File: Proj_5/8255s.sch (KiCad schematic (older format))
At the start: 6 parts, among them U1 8255, U2 8255, U3 8255

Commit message: Dont be wonky:
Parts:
- gave numbers to parts that had none: 3
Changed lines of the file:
@@
 $EndComp
 $Comp
-L Device:C C?
+L Device:C C3
 U 1 1 5EA6A7B2
 P 4750 3650
-F 0 "C?" V 4498 3650 50  0000 C CNN
+F 0 "C3" V 4498 3650 50  0000 C CNN
 F 1 "0.1uF" V 4589 3650 50  0000 C CNN
 F 2 "" H 4788 3500 50  0001 C CNN
@@
 $EndComp
 $Comp
-L Device:C C?
+L Device:C C4
 U 1 1 5EA6AA16
 P 8900 3500
-F 0 "C?" V 8648 3500 50  0000 C CNN
+F 0 "C4" V 8648 3500 50  0000 C CNN
 F 1 "0.1uF" V 8739 3500 50  0000 C CNN
 F 2 "" H 8938 3350 50  0001 C CNN
@@
 $EndComp
 $Comp
-L Device:C C?
+L Device:C C5
 U 1 1 5EA6B47A
 P 13150 3650
-F 0 "C?" V 12898 3650 50  0000 C CNN
+F 0 "C5" V 12898 3650 50  0000 C CNN
 F 1 "0.1uF" V 12989 3650 50  0000 C CNN
 F 2 "" H 13188 3500 50  0001 C CNN

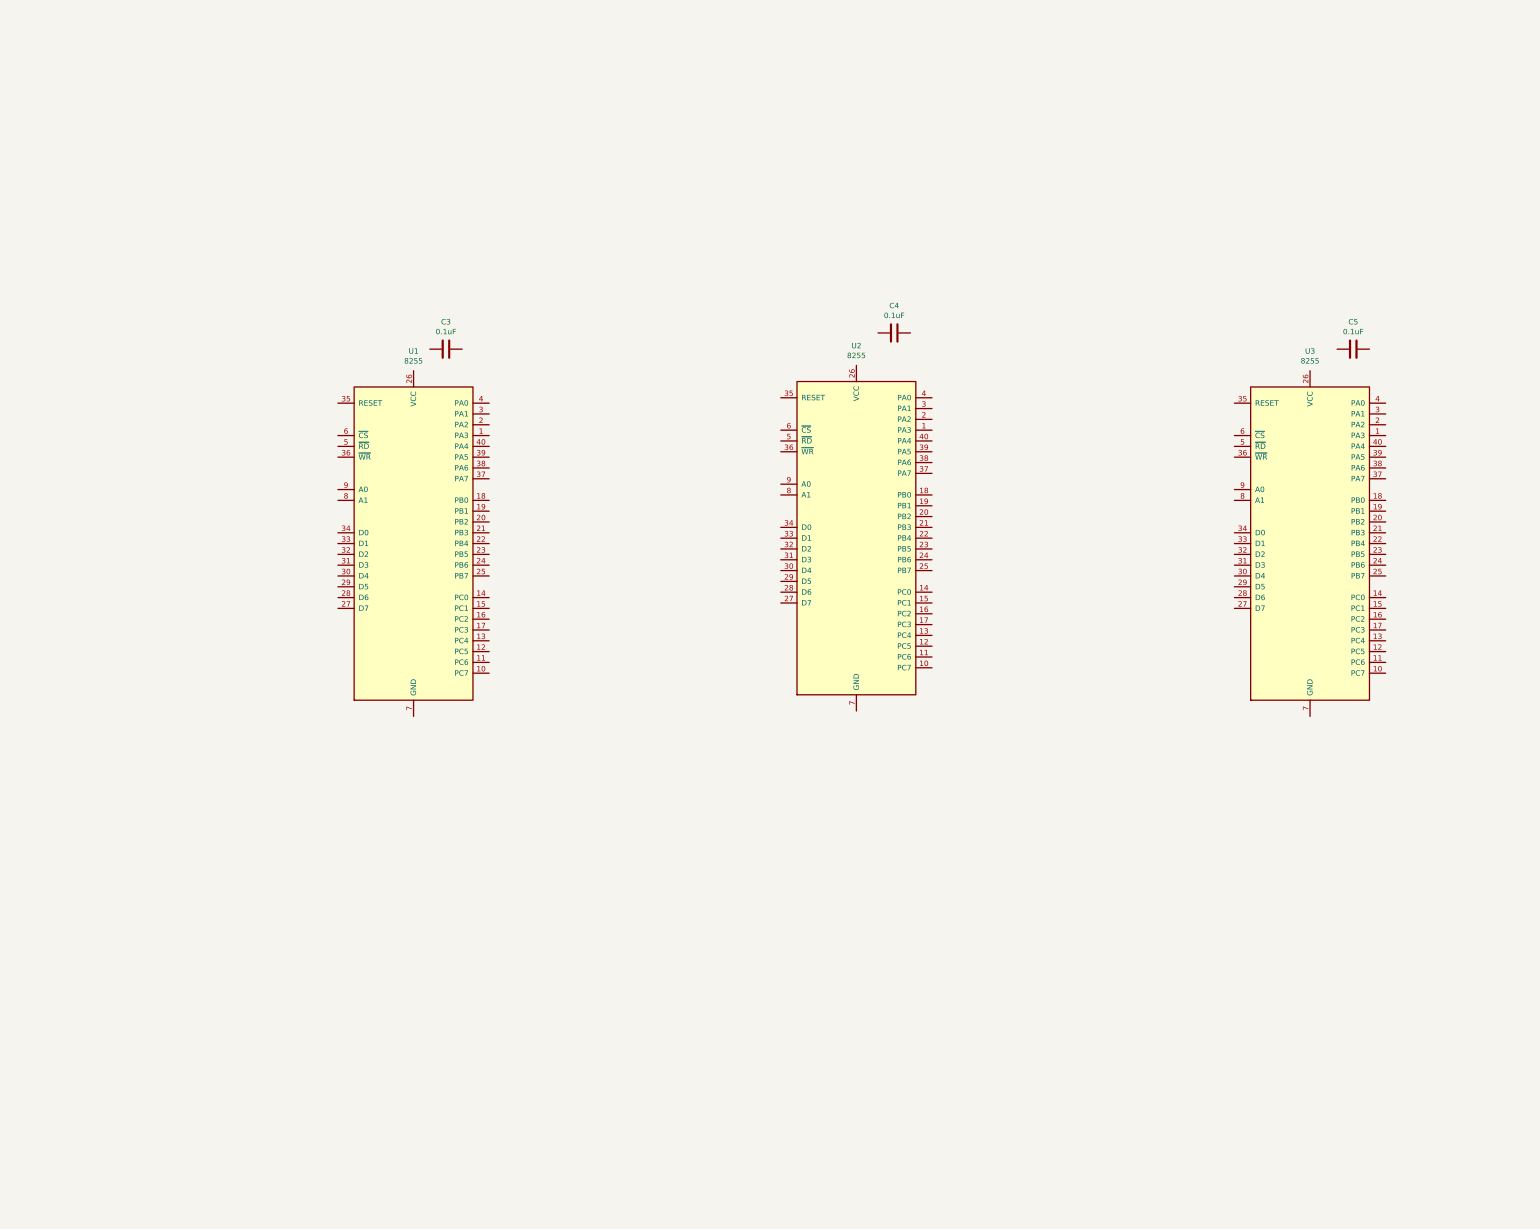
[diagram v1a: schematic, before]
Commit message: Made a rats nest in 8255.sch
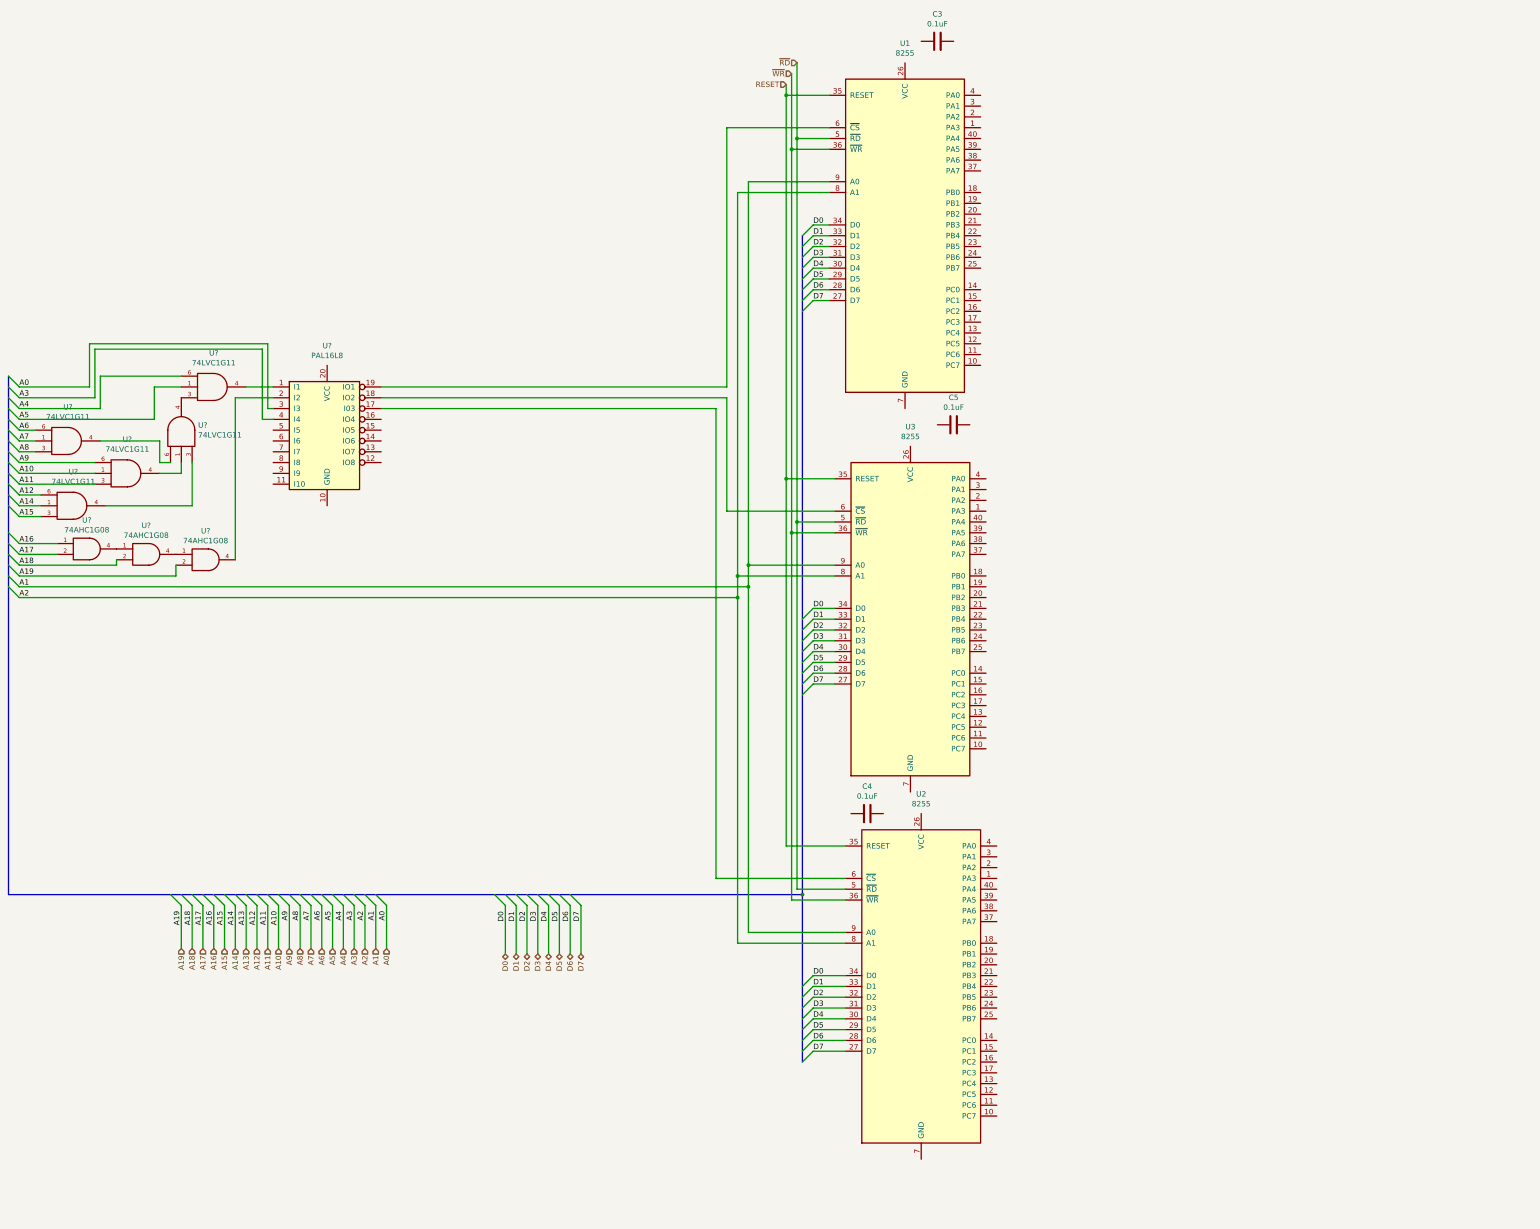
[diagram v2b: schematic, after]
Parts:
- added U?: PAL16L8, symbol Logic_Programmable:PAL16L8
- added U? (x3): 74AHC1G08, symbol 74xGxx:74AHC1G08
- added U? (x5): 74LVC1G11, symbol 74xGxx:74LVC1G11
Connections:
- net D7: now reaches U1.27 (D7)
- net D7: now also U2.27 (D7), U3.27 (D7)
- net D6: now reaches U1.28 (D6)
- net D6: now also U2.28 (D6), U3.28 (D6)
- net D5: now reaches U1.29 (D5)
- net D5: now also U2.29 (D5), U3.29 (D5)
- net D4: now reaches U1.30 (D4)
- net D4: now also U2.30 (D4), U3.30 (D4)
- net D3: now reaches U1.31 (D3)
- net D3: now also U2.31 (D3), U3.31 (D3)
- net D2: now reaches U1.32 (D2)
- net D2: now also U2.32 (D2), U3.32 (D2)
- net D1: now reaches U1.33 (D1)
- net D1: now also U2.33 (D1), U3.33 (D1)
- net D0: now reaches U1.34 (D0)
- net D0: now also U2.34 (D0), U3.34 (D0)
- net RESET: now reaches U1.35 (RESET)
- net RESET: now also U2.35 (RESET), U3.35 (RESET)
- net ~WR: now reaches U1.36 (~WR~)
- net ~WR: now also U2.36 (~WR~), U3.36 (~WR~)
- net ~RD: now reaches U1.5 (~RD~)
- net ~RD: now also U2.5 (~RD~), U3.5 (~RD~)
- net at U1.6 (~CS~): now also U?.19 (IO1)
- net A2: now reaches U1.8 (A1)
- net A2: now also U2.8 (A1), U3.8 (A1)
- net A1: now reaches U1.9 (A0)
- net A1: now also U2.9 (A0), U3.9 (A0)
- net at U2.6 (~CS~): now also U?.17 (I03)
- net at U3.6 (~CS~): now also U?.18 (IO2)
- new net: U?.1 (I1), U?.4
- new net: U?.2 (I2), U?.4
- new net: U?.1, U?.4 (x3)
- new net: U?.3, U?.4 (x2)
- new net: U?.4, U?.6
- new net A0: U?.3 (I3)
- new net A10: U?.1
- new net A11: U?.3
- new net A12: U?.6
- new net A14: U?.1
- new net A15: U?.3
- new net A16: U?.1
- new net A17: U?.2
- new net A18: U?.2
- new net A19: U?.2
- new net A3: U?.4 (I4)
- new net A4: U?.6
- new net A5: U?.1
- new net A6: U?.6
- new net A7: U?.1
- new net A8: U?.3
- new net A9: U?.6
- new net GND: U?.2 (GND), U?.2 (GND), U?.2 (GND), U?.2 (GND), U?.2 (GND), U?.3 (GND), U?.3 (GND), U?.3 (GND)
- new net VCC: U?.5 (VCC), U?.5 (VCC), U?.5 (VCC), U?.5 (VCC), U?.5 (VCC), U?.5 (VCC), U?.5 (VCC), U?.5 (VCC)
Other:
- moved on the sheet: C3, C4, C5, U1, U2, U3

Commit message: Sick wires bro
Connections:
- net M~IO: now reaches U?.5 (I5)
- no-connect marks 0 -> 10
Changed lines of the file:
@@
 $Descr A3 16535 11693
 encoding utf-8
-Sheet 3 9
+Sheet 9 9
 Title ""
 Date ""
@@
 Wire Wire Line
 	7950 1800 7950 5350
+NoConn ~ 3150 4500
+NoConn ~ 3150 4600
+NoConn ~ 3150 4700
+NoConn ~ 3150 4800
+NoConn ~ 3150 4900
+NoConn ~ 4150 4700
+NoConn ~ 4150 4600
+NoConn ~ 4150 4500
+NoConn ~ 4150 4400
+NoConn ~ 4150 4300
 Wire Bus Line
 	8050 8700 8050 10250
@@
 Wire Bus Line
 	700  8700 8050 8700
+Text HLabel 3150 4400 0    50   Input ~ 0
+M~IO
 $EndSCHEMATC

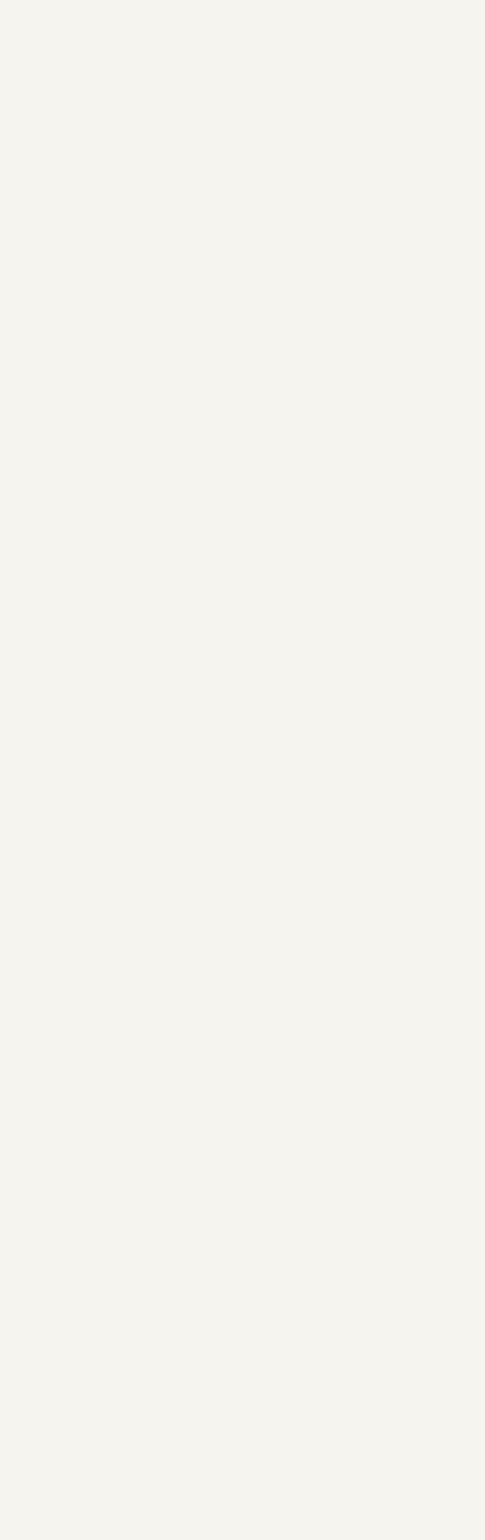
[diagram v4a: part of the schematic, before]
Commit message: Changes to Top Level Connections
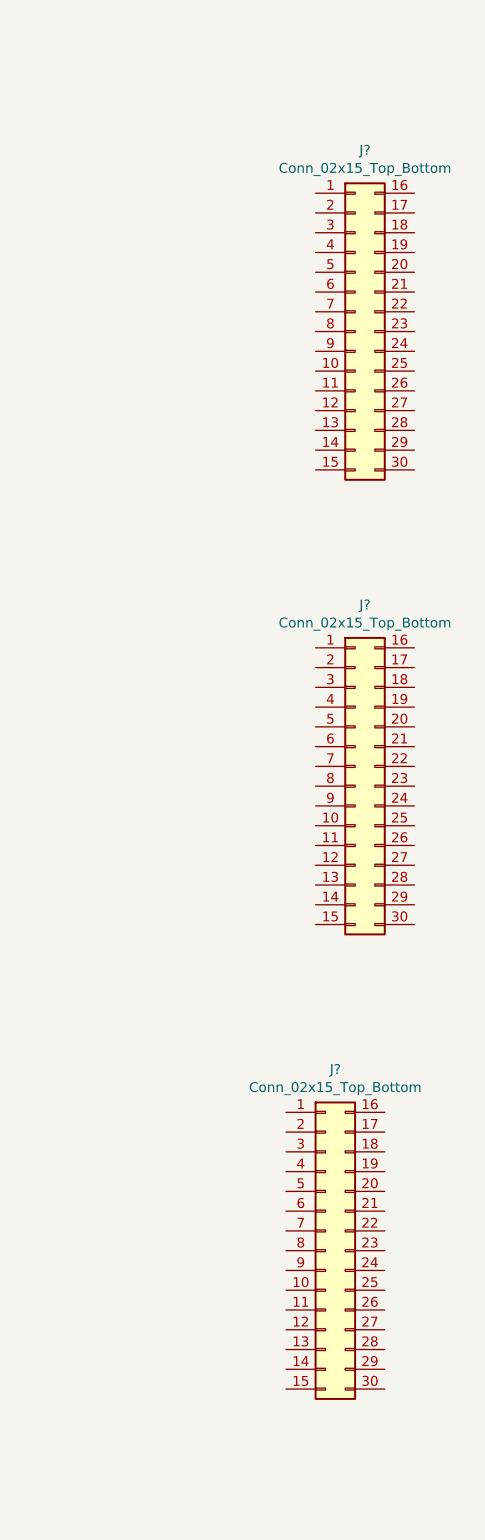
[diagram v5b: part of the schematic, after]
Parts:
- added J? (x3): Conn_02x15_Top_Bottom, symbol Connector_Generic:Conn_02x15_Top_Bottom
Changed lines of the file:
@@
 $Descr A3 16535 11693
 encoding utf-8
-Sheet 9 9
+Sheet 7 9
 Title ""
 Date ""
@@
 NoConn ~ 4150 4400
 NoConn ~ 4150 4300
+Text HLabel 3150 4400 0    50   Input ~ 0
+M~IO
+$Comp
+L Connector_Generic:Conn_02x15_Top_Bottom J?
+U 1 1 5F4C5EC4
+P 12000 2300
+F 0 "J?" H 12050 3217 50  0000 C CNN
+F 1 "Conn_02x15_Top_Bottom" H 12050 3126 50  0000 C CNN
+F 2 "" H 12000 2300 50  0001 C CNN
+F 3 "~" H 12000 2300 50  0001 C CNN
+	1    12000 2300
+	1    0    0    -1
+$EndComp
+$Comp
+L Connector_Generic:Conn_02x15_Top_Bottom J?
+U 1 1 5F4C897C
+P 12000 4600
+F 0 "J?" H 12050 5517 50  0000 C CNN
+F 1 "Conn_02x15_Top_Bottom" H 12050 5426 50  0000 C CNN
+F 2 "" H 12000 4600 50  0001 C CNN
+F 3 "~" H 12000 4600 50  0001 C CNN
+	1    12000 4600
+	1    0    0    -1
+$EndComp
+$Comp
+L Connector_Generic:Conn_02x15_Top_Bottom J?
+U 1 1 5F4CE164
+P 11850 6950
+F 0 "J?" H 11900 7867 50  0000 C CNN
+F 1 "Conn_02x15_Top_Bottom" H 11900 7776 50  0000 C CNN
+F 2 "" H 11850 6950 50  0001 C CNN
+F 3 "~" H 11850 6950 50  0001 C CNN
+	1    11850 6950
+	1    0    0    -1
+$EndComp
 Wire Bus Line
 	8050 8700 8050 10250
@@
 Wire Bus Line
 	700  8700 8050 8700
-Text HLabel 3150 4400 0    50   Input ~ 0
-M~IO
 $EndSCHEMATC
